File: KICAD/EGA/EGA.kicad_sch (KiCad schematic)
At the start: 16 parts, among them J1 12V, M1 Fan_3pin, Q1 IRLZ44N, U1 LM7805_TO220, U2 LM317_TO-220

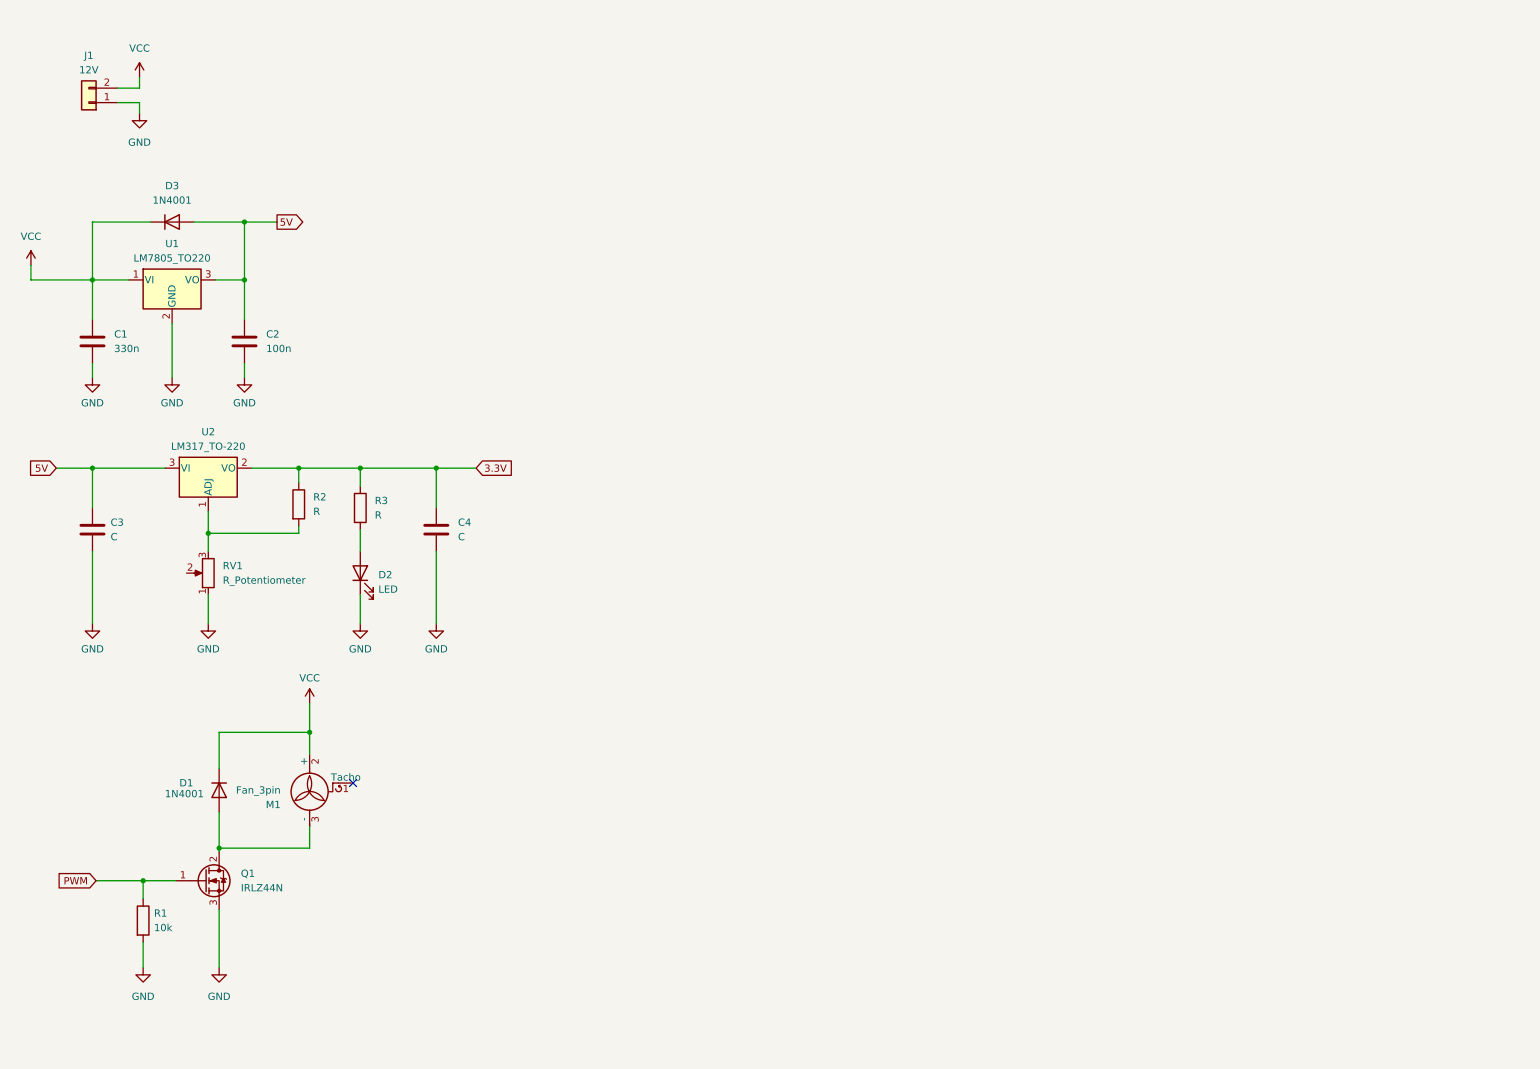
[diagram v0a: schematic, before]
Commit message: Agregado de lista de componentes con sus dimensiones, Tutorial de inclusion de libreria para simnolo y footprint
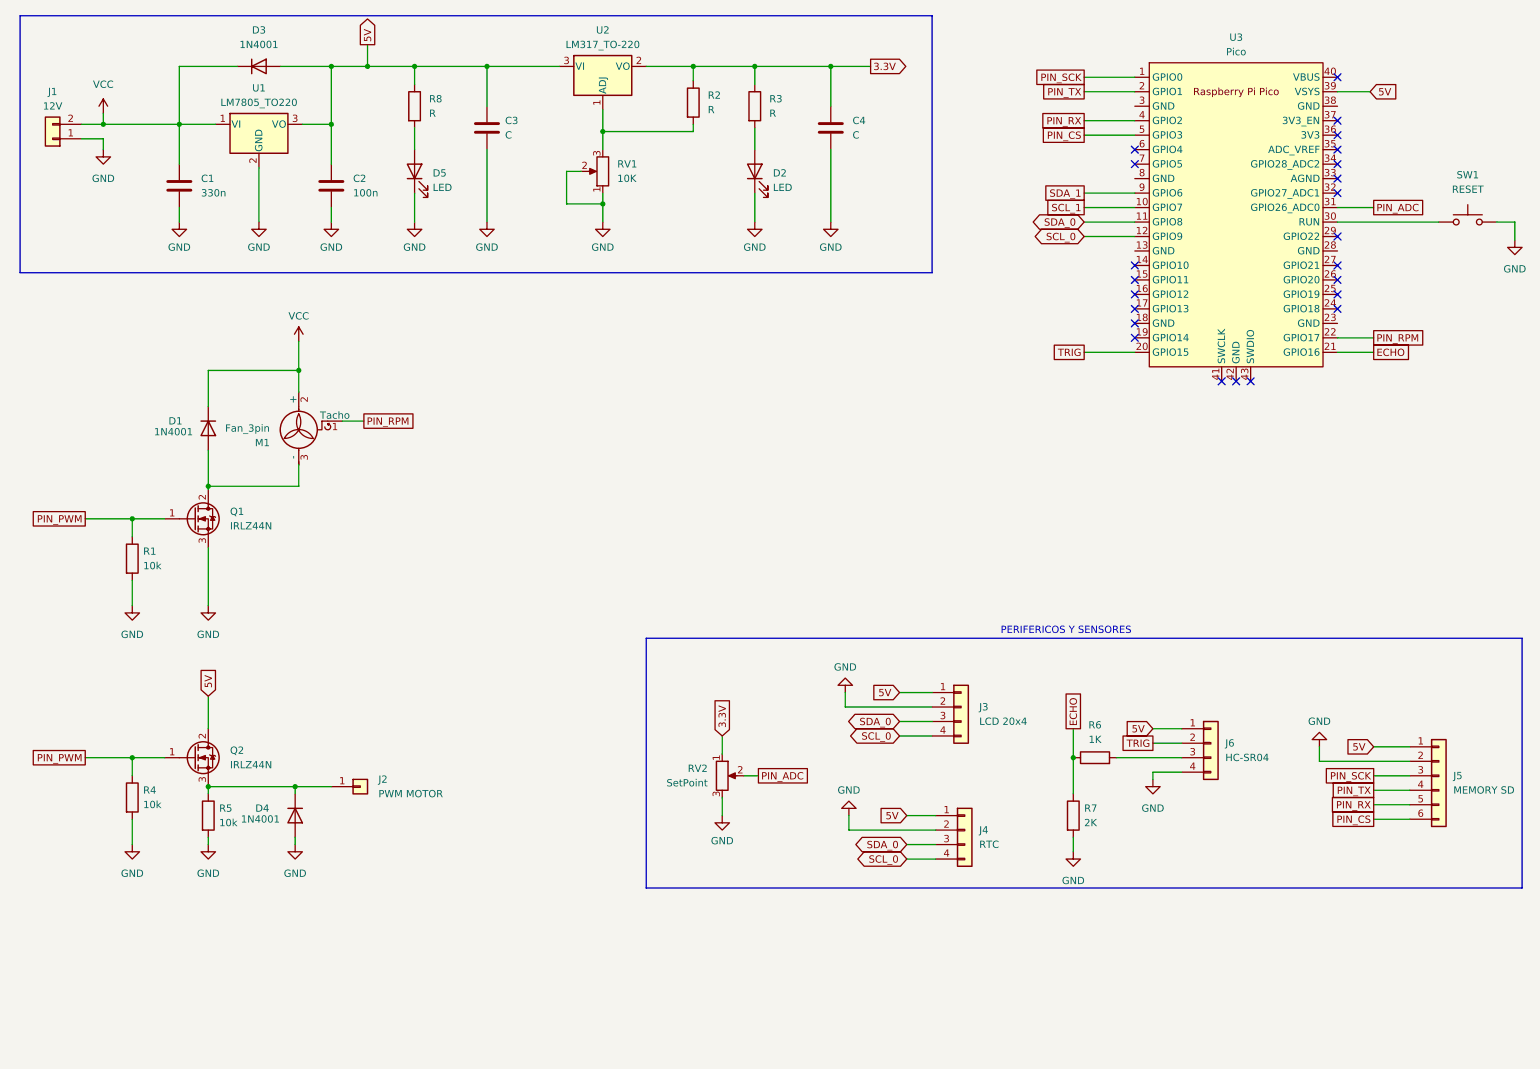
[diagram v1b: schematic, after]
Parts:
- added D4: 1N4001, Diode_THT:D_DO-41_SOD81_P10.16mm_Horizontal, symbol Diode:1N4001
- added D5: LED, symbol Device:LED
- added J2: PWM MOTOR, symbol Connector_Generic:Conn_01x01
- added J3: LCD 20x4, symbol Connector_Generic:Conn_01x04
- added J4: RTC, symbol Connector_Generic:Conn_01x04
- added J5: MEMORY SD, symbol Connector_Generic:Conn_01x06
- added J6: HC-SR04, symbol Connector_Generic:Conn_01x04
- added Q2: IRLZ44N, Package_TO_SOT_THT:TO-220-3_Vertical, symbol Transistor_FET:IRLZ44N
- added R4, R5: 10k, symbol Device:R
- added R6: 1K, symbol Device:R
- added R7: 2K, symbol Device:R
- added R8: R, symbol Device:R
- added RV2: SetPoint, symbol Device:R_Potentiometer
- added SW1: RESET, symbol Switch:SW_Push
- added U3: Pico, RPi_Pico:RPi_Pico_SMD_TH, symbol MCU_RaspberryPi_and_Boards:Pico
- C1: footprint (none) -> Capacitor_THT:C_Disc_D7.5mm_W4.4mm_P5.00mm
- C2: footprint (none) -> Capacitor_THT:C_Disc_D5.0mm_W2.5mm_P2.50mm
- RV1: value R_Potentiometer -> 10K
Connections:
- net 3.3V: now also RV2.1
- net 5V: now also J3.1 (Pin_1), J4.1 (Pin_1), J5.1 (Pin_1), J6.1 (Pin_1), Q2.2 (D), R8.1, U3.39 (VSYS)
- net GND: now also RV1.2, D4.2 (A), D5.1 (K), J3.2 (Pin_2), J4.2 (Pin_2), J5.2 (Pin_2), J6.4 (Pin_4), R4.2, R5.2, R7.2, RV2.3, SW1.2
- net PIN_RPM: now reaches M1.1 (Tacho)
- net PIN_RPM: now also U3.22 (GPIO17)
- net PWM renamed PIN_PWM
- net PIN_PWM: now also Q2.1 (G), R4.1
- new net: D5.2 (A), R8.2
- new net: J6.3 (Pin_3), R6.2
- new net: SW1.1, U3.30 (RUN)
- new net: D4.1 (K), J2.1 (Pin_1), Q2.3 (S), R5.1
- new net ECHO: R6.1, R7.1, U3.21 (GPIO16)
- new net PIN_ADC: RV2.2, U3.31 (GPIO26_ADC0)
- new net PIN_CS: J5.6 (Pin_6), U3.5 (GPIO3)
- new net PIN_RX: J5.5 (Pin_5), U3.4 (GPIO2)
- new net PIN_SCK: J5.3 (Pin_3), U3.1 (GPIO0)
- new net PIN_TX: J5.4 (Pin_4), U3.2 (GPIO1)
- new net SCL_0: J3.4 (Pin_4), J4.4 (Pin_4), U3.12 (GPIO9)
- new net SCL_1: U3.10 (GPIO7)
- new net SDA_0: J3.3 (Pin_3), J4.3 (Pin_3), U3.11 (GPIO8)
- new net SDA_1: U3.9 (GPIO6)
- new net TRIG: J6.2 (Pin_2), U3.20 (GPIO15)
- no-connect marks 1 -> 23
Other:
- note added: "PERIFERICOS Y SENSORES"
- moved on the sheet: C1, C2, C3, C4, D1, D2, D3, J1, M1, Q1, R1, R2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

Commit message: Actualizacion KICAD 13/7/2025
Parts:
- removed D1, D4: 1N4001, Diode_THT:D_DO-41_SOD81_P10.16mm_Horizontal, symbol Diode:1N4001
- removed J2: PWM MOTOR, symbol Connector_Generic:Conn_01x01
- removed M1: Fan_3pin, symbol Motor:Fan_3pin
- removed Q1, Q2: IRLZ44N, Package_TO_SOT_THT:TO-220-3_Vertical, symbol Transistor_FET:IRLZ44N
- removed R1, R4, R5: 10k, symbol Device:R
- added C2, C6, C7: 100n, Capacitor_THT:C_Disc_D5.0mm_W2.5mm_P2.50mm, symbol Device:C
- added D4, D5: LED, LED_THT:LED_D5.0mm, symbol Device:LED
- added H1, H2, H3, H4: MountingHole, MountingHole:MountingHole_2.1mm, symbol Mechanical:MountingHole
- added J6: FAN_12V_PWM_3.3V, Connector_PinHeader_2.00mm:PinHeader_1x04_P2.00mm_Vertical, symbol Connector_Generic:Conn_01x04
- added R6, R7: 100, Resistor_THT:R_Axial_DIN0204_L3.6mm_D1.6mm_P7.62mm_Horizontal, symbol Device:R
- added R8: 10K, Resistor_THT:R_Axial_DIN0204_L3.6mm_D1.6mm_P7.62mm_Horizontal, symbol Device:R
- added SW1: PAGINA, Button_Switch_THT:SW_PUSH_6mm_H4.3mm, symbol Switch:SW_Push
- C1: value 330n -> 100n; footprint Capacitor_THT:C_Disc_D7.5mm_W4.4mm_P5.00mm -> Capacitor_THT:C_Disc_D5.0mm_W2.5mm_P2.50mm
- C4: renamed from C3; value C -> 0.1uF; footprint (none) -> Capacitor_THT:C_Disc_D5.0mm_W2.5mm_P2.50mm
- C5: renamed from C4; value C -> 10uF; footprint (none) -> Capacitor_THT:CP_Radial_D5.0mm_P2.50mm; symbol Device:C -> Device:C_Polarized
- D2: renamed from D5; footprint (none) -> LED_THT:LED_D5.0mm
- D3: renamed from D2; footprint (none) -> LED_THT:LED_D5.0mm
- J1: footprint (none) -> Connector_Molex:Molex_KK-254_AE-6410-02A_1x02_P2.54mm_Vertical
- J2: renamed from J6; footprint (none) -> Connector_PinHeader_2.00mm:PinHeader_1x04_P2.00mm_Vertical
- J3, J4: footprint (none) -> Connector_PinHeader_2.00mm:PinHeader_1x04_P2.00mm_Vertical
- J5: footprint (none) -> Connector_PinHeader_2.00mm:PinHeader_1x06_P2.00mm_Vertical
- R1: renamed from R7; footprint (none) -> Resistor_THT:R_Axial_DIN0204_L3.6mm_D1.6mm_P7.62mm_Horizontal
- R2: renamed from R6; footprint (none) -> Resistor_THT:R_Axial_DIN0204_L3.6mm_D1.6mm_P7.62mm_Horizontal
- R3: renamed from R8; value R -> 330; footprint (none) -> Resistor_THT:R_Axial_DIN0204_L3.6mm_D1.6mm_P7.62mm_Horizontal
- R4: renamed from R2; value R -> 240; footprint (none) -> Resistor_THT:R_Axial_DIN0204_L3.6mm_D1.6mm_P7.62mm_Horizontal
- R5: renamed from R3; value R -> 240; footprint (none) -> Resistor_THT:R_Axial_DIN0204_L3.6mm_D1.6mm_P7.62mm_Horizontal
- RV1: renamed from RV2; footprint (none) -> Potentiometer_THT:Potentiometer_Vishay_T93XA_Horizontal
- RV2: renamed from RV1; value 10K -> 1K; footprint (none) -> Potentiometer_THT:Potentiometer_Vishay_T93YA_Vertical
- SW2: renamed from SW1; footprint (none) -> Button_Switch_THT:SW_PUSH_6mm_H4.3mm
- U3: footprint RPi_Pico:RPi_Pico_SMD_TH -> MCU_RaspberryPi_and_Boards:RPi_Pico_SMD_TH
- renumbered C2 to C3, D3 to D1
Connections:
- net 3.3V: now also R8.1
- net ECHO: now also U3.19 (GPIO14); no longer U3.21 (GPIO16)
- net GND: now also U3.3 (GND), C2.2, C6.2, C7.2, D4.1 (K), D5.1 (K), J6.1 (Pin_1), SW1.2; no longer SW2.2
- net PIN_ADC: now also C2.1
- net PIN_PWM: now also U3.15 (GPIO11), J6.4 (Pin_4)
- net PIN_RPM: now also U3.14 (GPIO10); no longer U3.22 (GPIO17)
- net VCC: now also C6.1, C7.1, J6.2 (Pin_2)
- net MAX_ALTURA: now reaches U3.16 (GPIO12)
- net MAX_ALTURA: now also R7.1
- net MIN_ALTURA: now reaches U3.17 (GPIO13)
- net MIN_ALTURA: now also R6.1
- net at U3.38 (GND): now also SW2.2
- new net: D4.2 (A), R6.2
- new net: D5.2 (A), R7.2
- new net PIN_PAGINA: R8.2, SW1.1, U3.21 (GPIO16)
- new net PIN_PRM: J6.3 (Pin_3)
- no-connect marks 23 -> 18
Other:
- note added: "ALIMENTACION DE 12V, 5V , 3.3V"
- note added: "MODULOS"
- note removed: "PERIFERICOS Y SENSORES"
- moved on the sheet: C3, C4, D1, D2, D3, J1, J2, J3, J4, J5, R1, R2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

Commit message: Adicion de PCB_Preliminar para entregar en la segunda parte
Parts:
- removed J5: MEMORY SD, Connector_PinHeader_2.00mm:PinHeader_1x06_P2.00mm_Vertical, symbol Connector_Generic:Conn_01x06
- added J7: SD CARD, Connector_PinHeader_2.54mm:PinHeader_1x08_P2.54mm_Vertical, symbol Connector_Generic:Conn_01x08
- J2, J3, J4, J6: footprint Connector_PinHeader_2.00mm:PinHeader_1x04_P2.00mm_Vertical -> Connector_PinHeader_2.54mm:PinHeader_1x04_P2.54mm_Vertical
- SW1, SW2: footprint Button_Switch_THT:SW_PUSH_6mm_H4.3mm -> Button_Switch_THT:SW_PUSH_6mm_H5mm
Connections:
- net PIN_PRM is gone; now on net PIN_RPM: J6.3 (Pin_3)
- net 5V: now also J7.3 (Pin_3)
- net GND: now also U3.13 (GND), U3.18 (GND), U3.23 (GND), U3.8 (GND), J7.1 (Pin_1), J7.8 (Pin_8); no longer U3.3 (GND)
- net PIN_CS: now also J7.4 (Pin_4)
- net PIN_PWM: now also U3.14 (GPIO10); no longer U3.15 (GPIO11)
- net PIN_RPM: now also U3.15 (GPIO11); no longer U3.14 (GPIO10)
- net PIN_SCK: now also J7.6 (Pin_6)
- net PIN_RX renamed PIN_RX_MISO
- net PIN_RX_MISO: now also J7.7 (Pin_7)
- net PIN_TX renamed PIN_TX_MOSI
- net PIN_TX_MOSI: now also J7.5 (Pin_5)
- no-connect marks 18 -> 21
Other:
- moved on the sheet: J1

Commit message: Actualizacion de EGA en KICAD
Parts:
- removed R1: 2K, Resistor_THT:R_Axial_DIN0204_L3.6mm_D1.6mm_P7.62mm_Horizontal, symbol Device:R
- removed R2: 1K, Resistor_THT:R_Axial_DIN0204_L3.6mm_D1.6mm_P7.62mm_Horizontal, symbol Device:R
- added J10: TEST_TRIG, Connector_PinHeader_2.54mm:PinHeader_1x01_P2.54mm_Vertical, symbol Connector_Generic:Conn_01x01
- added J5: TEST_PWM, Connector_PinHeader_2.54mm:PinHeader_1x01_P2.54mm_Vertical, symbol Connector_Generic:Conn_01x01
- added J8: TEST_RPM, Connector_PinHeader_2.54mm:PinHeader_1x01_P2.54mm_Vertical, symbol Connector_Generic:Conn_01x01
- added J9: TEST_ECHO, Connector_PinHeader_2.54mm:PinHeader_1x01_P2.54mm_Vertical, symbol Connector_Generic:Conn_01x01
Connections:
- net ECHO: now also J2.3 (Pin_3), U3.20 (GPIO15), J9.1 (Pin_1); no longer U3.19 (GPIO14)
- net GND: no longer J7.1 (Pin_1), U3.13 (GND), U3.18 (GND), U3.23 (GND), U3.8 (GND)
- net PIN_PAGINA: now also U3.24 (GPIO18); no longer U3.21 (GPIO16)
- net PIN_PWM: now also J5.1 (Pin_1)
- net PIN_RPM: now also J8.1 (Pin_1)
- net TRIG: now also U3.19 (GPIO14), J10.1 (Pin_1); no longer U3.20 (GPIO15)
- net UART_RX: now reaches U3.22 (GPIO17)
- new net UART_TX: U3.21 (GPIO16)
- no-connect marks 21 -> 24
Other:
- moved on the sheet: D4, D5, H1, H2, H3, H4, J1, R6, R7, R8, SW1, SW2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

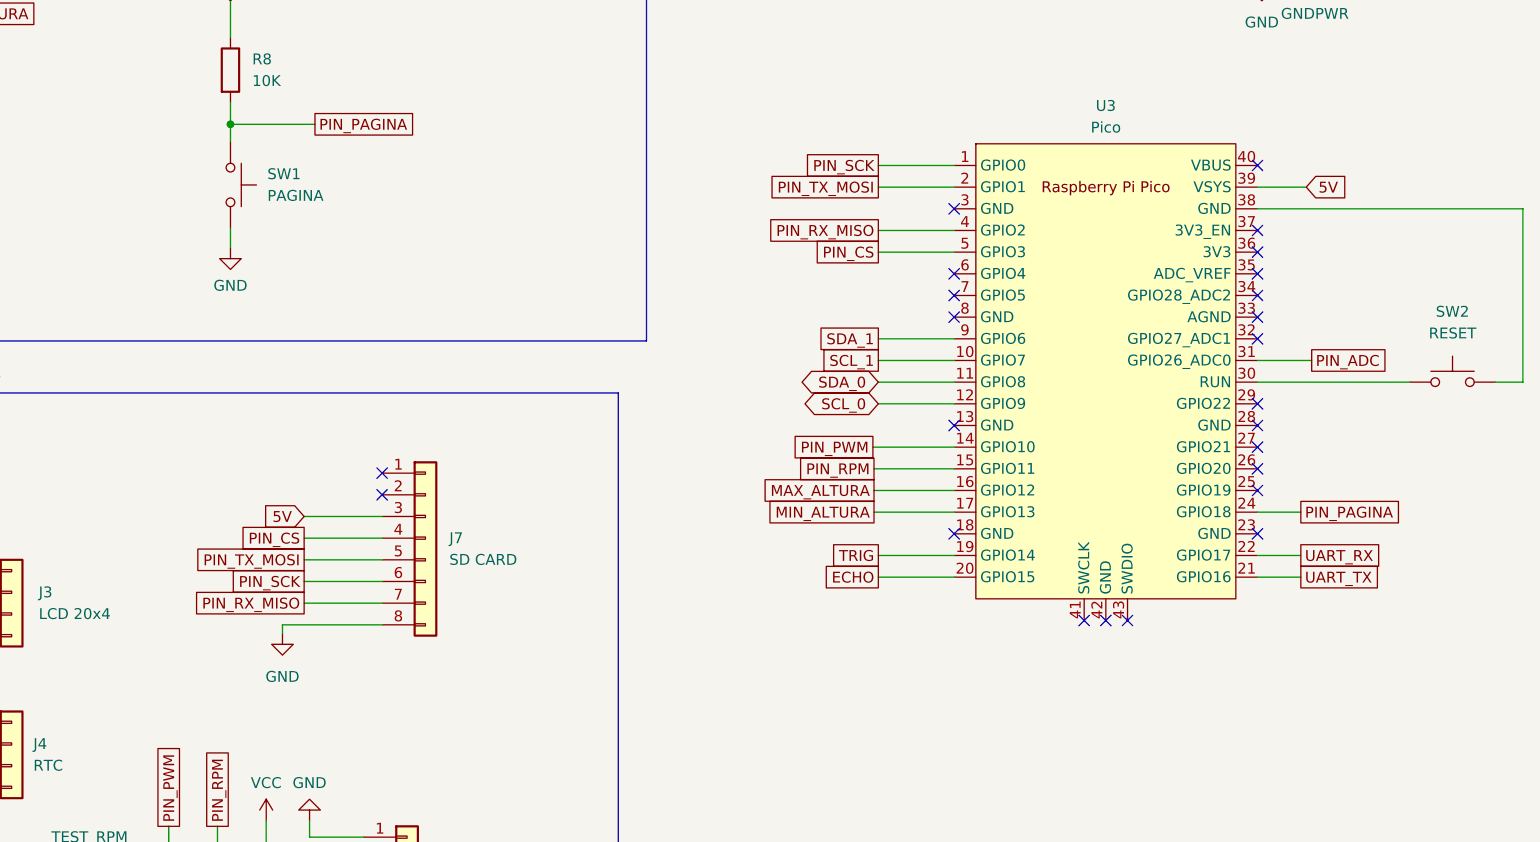
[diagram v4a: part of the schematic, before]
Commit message: Actualizacion KICAD, CAmbio de pines en UART, los pines de I2C se mantienen sin cambios
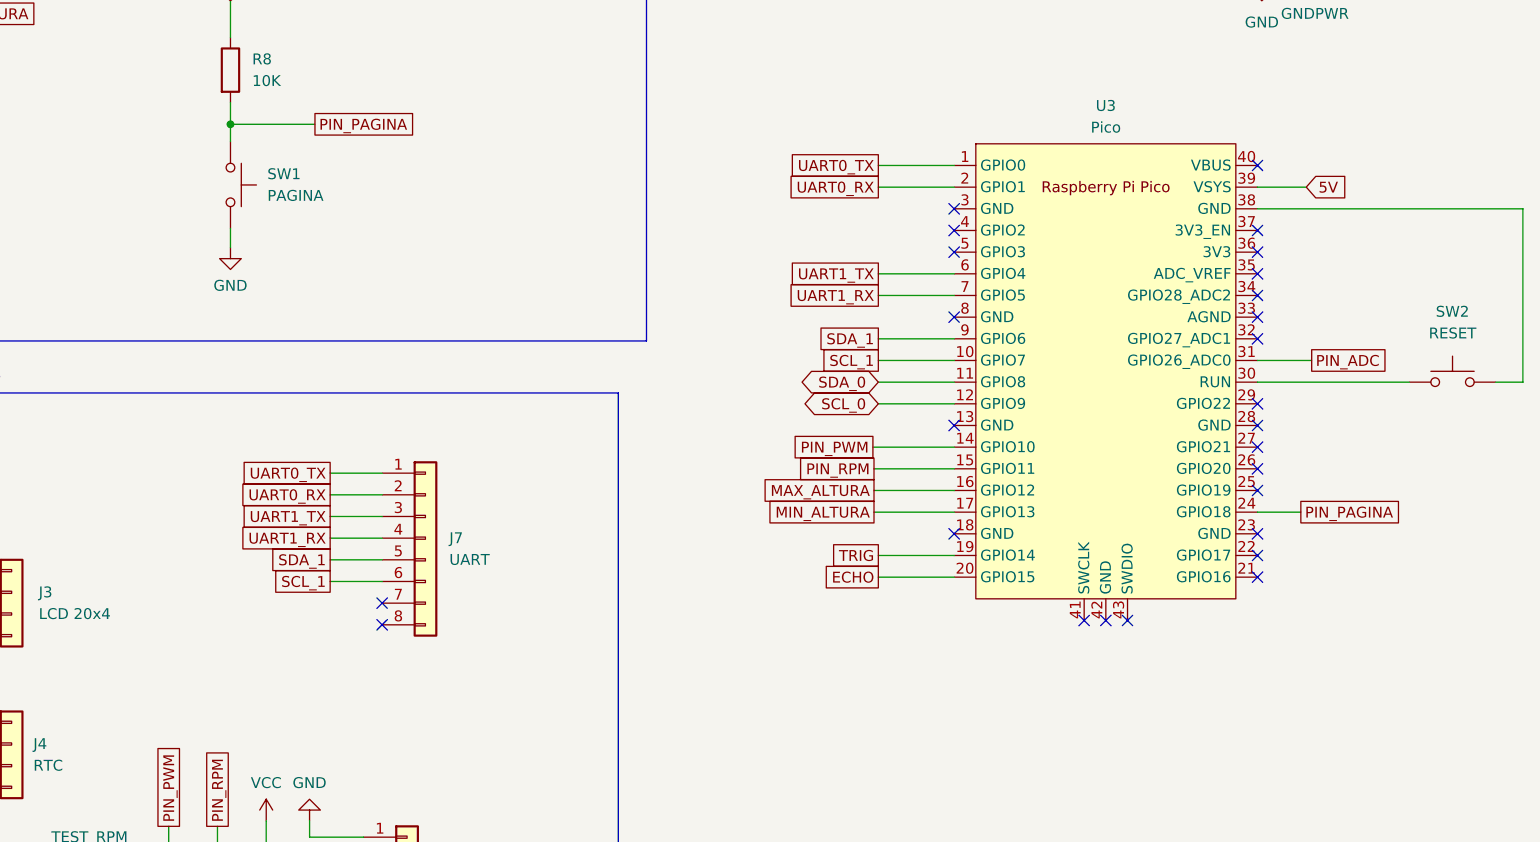
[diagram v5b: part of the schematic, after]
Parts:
- J7: value SD CARD -> UART
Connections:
- net 5V: no longer J7.3 (Pin_3)
- net GND: no longer J7.8 (Pin_8)
- net SCL_1: now also J7.6 (Pin_6)
- net SDA_1: now also J7.5 (Pin_5)
- net UART1_TX: now reaches U3.6 (GPIO4)
- net UART1_TX: now also J7.3 (Pin_3)
- net UART1_RX: now reaches U3.7 (GPIO5)
- net UART1_RX: now also J7.4 (Pin_4)
- net UART0_TX: now reaches J7.1 (Pin_1)
- net UART0_TX: now also U3.1 (GPIO0)
- net UART0_RX: now reaches J7.2 (Pin_2)
- net UART0_RX: now also U3.2 (GPIO1)
- net PIN_CS: no longer names the net of U3.5 (GPIO3)
- net PIN_CS: no longer J7.4 (Pin_4)
- net PIN_RX_MISO: no longer names the net of U3.4 (GPIO2)
- net PIN_RX_MISO: no longer J7.7 (Pin_7)
- removed net PIN_SCK: J7.6 (Pin_6), U3.1 (GPIO0)
- removed net PIN_TX_MOSI: J7.5 (Pin_5), U3.2 (GPIO1)
- net UART_RX: no longer names the net of U3.22 (GPIO17)
- net UART_TX: no longer names the net of U3.21 (GPIO16)
- no-connect marks 24 -> 26
